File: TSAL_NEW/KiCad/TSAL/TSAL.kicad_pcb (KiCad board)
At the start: 2 copper layers, 101.6 x 25.4 mm, 0 parts

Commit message: Ready for Review
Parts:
- added C1: 1u, Capacitor_SMD:C_0603_1608Metric_Pad1.05x0.95mm_HandSolder, F.Cu at (174.5, 113.7)
- added C2: 1u, Capacitor_SMD:C_0603_1608Metric_Pad1.05x0.95mm_HandSolder, F.Cu at (174.6, 115.4)
- added J1: HV INPUT, Connector_TE-Connectivity:TE_MATE-N-LOK_1-770866-x_1x02_P4.14mm_Vertical, F.Cu at (120.3, 94.0)
- added J2: HV GND, Connector_TE-Connectivity:TE_MATE-N-LOK_1-770866-x_1x02_P4.14mm_Vertical, F.Cu at (119.8, 120.9)
- added J3: Green_LED_Jp, Connector_TE-Connectivity:TE_MATE-N-LOK_1-770866-x_1x02_P4.14mm_Vertical, F.Cu at (178.4, 94.0)
- added J4: Conn_02x03_Counter_Clockwise, Connector_TE-Connectivity:TE_MATE-N-LOK_1-770875-x_2x03_P4.14mm_Vertical, F.Cu at (194.6, 103.4)
- added Q1: BSS84, Package_TO_SOT_SMD:SOT-23, F.Cu at (180.8, 113.9)
- added Q2: FDD8447L, Package_TO_SOT_SMD:TO-252-2, F.Cu at (196.2, 117.8)
- added R1: 10k, Resistor_SMD:R_0603_1608Metric_Pad1.05x0.95mm_HandSolder, F.Cu at (144.4, 123.7)
- added R2: 180k, Resistor_SMD:R_0603_1608Metric_Pad1.05x0.95mm_HandSolder, F.Cu at (136.8, 103.9)
- added R3: 20k, Resistor_SMD:R_0603_1608Metric_Pad1.05x0.95mm_HandSolder, F.Cu at (131.9, 103.9)
- added R4: 100k, Resistor_SMD:R_0603_1608Metric_Pad1.05x0.95mm_HandSolder, F.Cu at (183.1, 118.4)
- added R5: 235k, Resistor_SMD:R_0603_1608Metric_Pad1.05x0.95mm_HandSolder, F.Cu at (183.1, 122.0)
- added R6: R, Resistor_SMD:R_0603_1608Metric_Pad1.05x0.95mm_HandSolder, F.Cu at (182.5, 110.7)
- added R7: 10k, Resistor_SMD:R_0603_1608Metric_Pad1.05x0.95mm_HandSolder, F.Cu at (191.0, 121.7)
- added R8: 1k, Resistor_SMD:R_0603_1608Metric_Pad1.05x0.95mm_HandSolder, F.Cu at (190.9, 114.0)
- added U1: LTV-817S, Package_DIP:SMDIP-4_W9.53mm, F.Cu at (136.0, 121.7)
- added U2: LR8K4-G, Package_TO_SOT_SMD:TO-252-2, F.Cu at (135.1, 96.0)
- added U3: LM555, Package_SO:SOIC-8_3.9x4.9mm_P1.27mm, F.Cu at (177.0, 119.6)
- added U4: LDB-350L, aero_footprint:LDB-_L, F.Cu at (167.0, 93.1)
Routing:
- net +12V: track 0.00 -> 81.8 mm
- net /GLV+: track 0.00 -> 79.7 mm
- net +24V: track 0.00 -> 64.5 mm
- net GNDA: track 0.00 -> 38.0 mm
- net +12VA: track 0.00 -> 27.4 mm
- net /555_OUTPUT: track 0.00 -> 20.5 mm
- net /THR: track 0.00 -> 19.4 mm
- net /HV+: track 0.00 -> 14.8 mm
- net /LED_GREEN+: track 0.00 -> 12.5 mm
- net /LED_RED+: track 0.00 -> 10.3 mm
- net Net-(R2-Pad2): track 0.00 -> 9.45 mm
- net /DIS: track 0.00 -> 5.65 mm
- net Net-(Q2-Pad3): track 0.00 -> 3.70 mm
- net Net-(Q1-Pad3): track 0.00 -> 2.53 mm
- added copper zone on F.Cu, net GND
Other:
- board size 101.6 x 25.4 mm -> 96.5 x 40.6 mm
- net class HV added: clearance 0.85, trace_width 1.2, via_dia 1, via_drill 0.6
- board text added: "GLV"
- board text added: "HV+"
- board text added: "HV-"
- board text added: "TSV"

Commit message: Ready for Review
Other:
- board text added: "TSAL G.Spearing 20.0131"
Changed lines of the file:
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@@
   (general
     (thickness 1.6)
-    (drawings 18)
+    (drawings 19)
     (tracks 93)
     (zones 0)
@@
   )
   (setup
-    (last_trace_width 0.65)
+    (last_trace_width 0.25)
     (user_trace_width 0.24)
     (user_trace_width 0.36)
@@
     (add_net +12V)
     (add_net +24V)
-    (add_net /12V)
     (add_net /555_OUTPUT)
     (add_net /DIS)
@@
     (add_net "Net-(Q2-Pad3)")
     (add_net "Net-(R2-Pad2)")
-    (add_net "Net-(U3-Pad5)")
-    (add_net "Net-(U4-Pad21)")
   )
   (net_class HV ""
@@
     )
   )
+  (gr_text "TSAL\nG.Spearing\n20.0131" (at 191.77 120.65) (layer B.SilkS)
+    (effects (font (size 1 1) (thickness 0.15)) (justify mirror))
+  )
   (gr_line (start 136.398 126.619) (end 136.398 118.364) (layer F.SilkS) (width 0.5))

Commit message: Ready for Reivew
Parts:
- added G***: LOGO, aero_footprint:AERO_Logo_25x10mm, B.Cu at (175.0, 110.7)
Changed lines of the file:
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@@
     (tracks 93)
     (zones 0)
-    (modules 20)
+    (modules 21)
     (nets 16)
   )
@@
     (add_net GNDA)
   )
+  (module aero_footprint:AERO_Logo_25x10mm (layer B.Cu)
+    (at 175.006 110.744 180)
+    (fp_text reference G*** (at 0 0) (layer B.SilkS) hide
+      (effects (font (size 1.524 1.524) (thickness 0.3)) (justify mirror))
+    )
+    (fp_text value LOGO (at 0.75 0) (layer B.SilkS) hide
+      (effects (font (size 1.524 1.524) (thickness 0.3)) (justify mirror))
+    )
+    (fp_poly (pts (xy 12.525229 2.710159) (xy 12.525229 -2.535324) (xy 10.339393 -4.71889) (xy 9.364192 -3.742421)
+      (xy 8.388991 -2.765953) (xy 8.388991 -2.2956) (xy 9.845413 -2.2956) (xy 10.032432 -2.488555)
+      (xy 10.219452 -2.68151) (xy 11.01055 -1.896474) (xy 11.01055 2.012048) (xy 10.427982 2.592431)
+      (xy 9.845413 3.172814) (xy 9.845413 -2.2956) (xy 8.388991 -2.2956) (xy 8.388991 2.76845)
+      (xy 9.408495 3.786706) (xy 10.427999 4.804961) (xy 12.525229 2.710159)) (layer B.SilkS) (width 0.01))
+    (fp_poly (pts (xy 6.802244 3.946175) (xy 7.631651 3.115285) (xy 7.631651 1.604369) (xy 7.123086 1.093437)
+      (xy 6.614521 0.582504) (xy 7.152215 0.042566) (xy 7.689908 -0.497373) (xy 7.689908 -2.763538)
+      (xy 7.994602 -3.072064) (xy 8.299295 -3.38059) (xy 6.960436 -4.719449) (xy 6.307049 -4.063738)
+      (xy 5.653662 -3.408028) (xy 6.228442 -2.767202) (xy 6.233486 -1.250536) (xy 5.592661 -0.611697)
+      (xy 4.951835 0.027141) (xy 4.951835 -2.829839) (xy 5.243762 -3.117377) (xy 5.53569 -3.404915)
+      (xy 4.880607 -4.061861) (xy 4.656022 -4.284832) (xy 4.45981 -4.475378) (xy 4.306705 -4.619528)
+      (xy 4.21144 -4.703309) (xy 4.187859 -4.718807) (xy 4.136831 -4.678799) (xy 4.020352 -4.568311)
+      (xy 3.852889 -4.401644) (xy 3.648913 -4.193102) (xy 3.512625 -4.05132) (xy 2.875057 -3.383832)
+      (xy 3.495413 -2.771182) (xy 3.495413 0.787039) (xy 4.835321 0.787039) (xy 6.3203 2.272018)
+      (xy 5.577811 3.014508) (xy 4.835321 3.756998) (xy 4.835321 0.787039) (xy 3.495413 0.787039)
+      (xy 3.495413 2.938594) (xy 3.161895 3.275628) (xy 2.828378 3.612662) (xy 3.98841 4.777064)
+      (xy 5.972837 4.777064) (xy 6.802244 3.946175)) (layer B.SilkS) (width 0.01))
+    (fp_poly (pts (xy -2.477659 2.622121) (xy -3.029276 2.068201) (xy -3.580892 1.514282) (xy -5.184862 3.115182)
+      (xy -5.184862 0.69421) (xy -4.078692 0.711211) (xy -2.972522 0.728211) (xy -4.396646 -0.699083)
+      (xy -5.184862 -0.699083) (xy -5.184862 -2.382603) (xy -4.977207 -2.540989) (xy -4.769551 -2.699376)
+      (xy -4.175481 -2.107328) (xy -3.581411 -1.515279) (xy -2.530301 -2.566389) (xy -3.611941 -3.642598)
+      (xy -3.902517 -3.930701) (xy -4.165689 -4.189694) (xy -4.390326 -4.40878) (xy -4.565301 -4.577165)
+      (xy -4.679482 -4.684053) (xy -4.72142 -4.718807) (xy -4.768729 -4.679379) (xy -4.886204 -4.568805)
+      (xy -5.061953 -4.398654) (xy -5.284083 -4.180497) (xy -5.540701 -3.925902) (xy -5.695272 -3.77149)
+      (xy -6.641284 -2.824173) (xy -6.641284 2.704844) (xy -5.623333 3.72851) (xy -4.605381 4.752177)
+      (xy -2.477659 2.622121)) (layer B.SilkS) (width 0.01))
+    (fp_poly (pts (xy -8.694247 3.771558) (xy -7.689908 2.765987) (xy -7.689908 -2.763538) (xy -7.385215 -3.072064)
+      (xy -7.080521 -3.38059) (xy -7.749951 -4.050019) (xy -8.41938 -4.719449) (xy -9.755082 -3.379947)
+      (xy -9.450706 -3.071743) (xy -9.14633 -2.763538) (xy -9.14633 -1.572936) (xy -10.427982 -1.572936)
+      (xy -10.427982 -2.763538) (xy -10.123288 -3.072064) (xy -9.818595 -3.38059) (xy -11.157454 -4.719449)
+      (xy -11.825305 -4.049698) (xy -12.493155 -3.379947) (xy -12.18878 -3.071743) (xy -11.884404 -2.763538)
+      (xy -11.884404 -0.058257) (xy -10.427982 -0.058257) (xy -9.14633 -0.058257) (xy -9.14633 1.838329)
+      (xy -9.784204 2.506665) (xy -10.422078 3.175) (xy -10.42503 1.558371) (xy -10.427982 -0.058257)
+      (xy -11.884404 -0.058257) (xy -11.884404 2.593581) (xy -10.791495 3.685355) (xy -9.698586 4.777128)
+      (xy -8.694247 3.771558)) (layer B.SilkS) (width 0.01))
+    (fp_poly (pts (xy 1.48555 3.437156) (xy 0.88742 1.805963) (xy 1.792647 1.805963) (xy 2.13411 1.805266)
+      (xy 2.374206 1.801911) (xy 2.528081 1.794001) (xy 2.610878 1.779642) (xy 2.637744 1.756938)
+      (xy 2.623822 1.723993) (xy 2.607124 1.704014) (xy 2.560496 1.642703) (xy 2.452739 1.496064)
+      (xy 2.2906 1.273472) (xy 2.080823 0.984301) (xy 1.830152 0.637926) (xy 1.545334 0.243722)
+      (xy 1.233113 -0.188937) (xy 0.900234 -0.650674) (xy 0.553443 -1.132116) (xy 0.199483 -1.623887)
+      (xy -0.154899 -2.116613) (xy -0.502959 -2.600919) (xy -0.837952 -3.06743) (xy -1.153132 -3.506771)
+      (xy -1.441755 -3.909568) (xy -1.697076 -4.266444) (xy -1.912349 -4.568027) (xy -2.08083 -4.80494)
+      (xy -2.195773 -4.967808) (xy -2.250434 -5.047258) (xy -2.251631 -5.049138) (xy -2.247031 -5.018182)
+      (xy -2.207458 -4.887527) (xy -2.136353 -4.667475) (xy -2.037157 -4.368325) (xy -1.913312 -4.000379)
+      (xy -1.768257 -3.573937) (xy -1.605433 -3.099301) (xy -1.450599 -2.651135) (xy -1.272624 -2.137289)
+      (xy -1.106931 -1.658286) (xy -0.957313 -1.225136) (xy -0.827562 -0.84885) (xy -0.721473 -0.540437)
+      (xy -0.642839 -0.310908) (xy -0.595452 -0.171273) (xy -0.582569 -0.131524) (xy -0.637453 -0.126278)
+      (xy -0.788619 -0.121831) (xy -1.015833 -0.118534) (xy -1.298863 -0.116739) (xy -1.448313 -0.116514)
+      (xy -2.314057 -0.116514) (xy -1.663387 1.354472) (xy -1.457671 1.81999) (xy -1.235644 2.323191)
+      (xy -1.011221 2.832488) (xy -0.798318 3.316289) (xy -0.610849 3.743005) (xy -0.521442 3.946904)
+      (xy -0.030166 5.068348) (xy 2.083681 5.068348) (xy 1.48555 3.437156)) (layer B.SilkS) (width 0.01))
+  )
   (module Connector_TE-Connectivity:TE_MATE-N-LOK_1-770866-x_1x02_P4.14mm_Vertical (layer F.Cu)

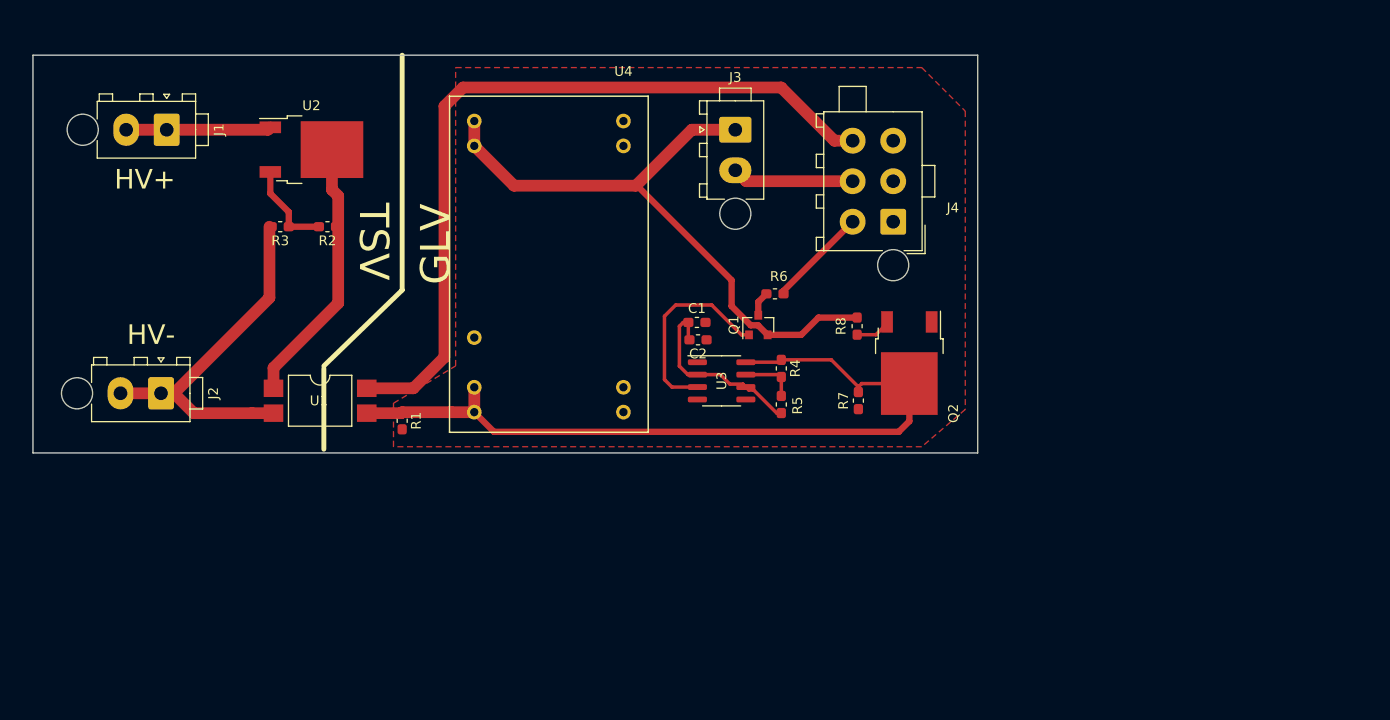
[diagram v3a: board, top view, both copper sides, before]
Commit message: Final Schem - No Boost
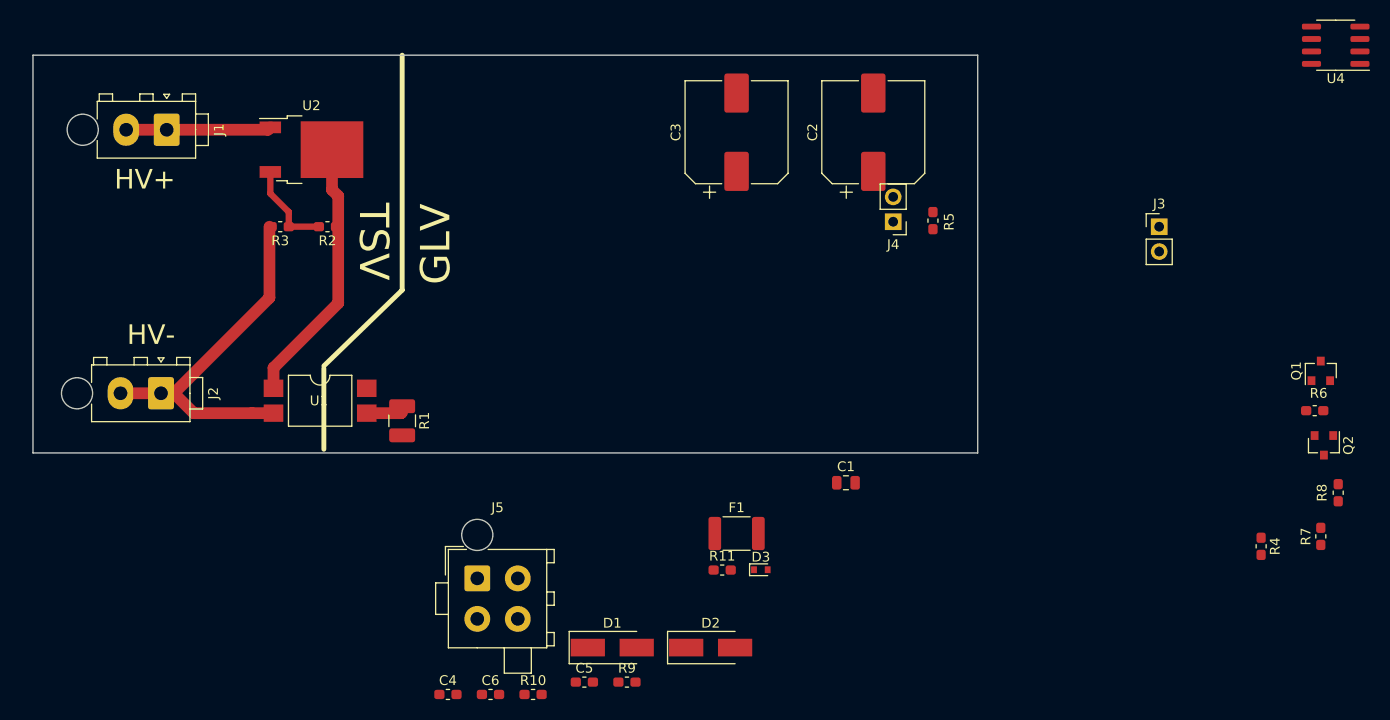
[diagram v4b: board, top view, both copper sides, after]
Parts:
- removed G***: LOGO, aero_footprint:AERO_Logo_25x10mm
- removed U3: LM555, Package_SO:SOIC-8_3.9x4.9mm_P1.27mm
- added C3: 330uF, Capacitor_SMD:CP_Elec_10x10, F.Cu at (178.6, 94.2)
- added C4: 1u, Capacitor_SMD:C_0603_1608Metric_Pad1.05x0.95mm_HandSolder, F.Cu at (149.1, 151.7)
- added C5: 1u, Capacitor_SMD:C_0603_1608Metric_Pad1.05x0.95mm_HandSolder, F.Cu at (163.0, 150.4)
- added C6: 0.1uF, Capacitor_SMD:C_0603_1608Metric_Pad1.05x0.95mm_HandSolder, F.Cu at (153.4, 151.7)
- added D1: B340A-13-F1, Diode_SMD:D_SMA_Handsoldering, F.Cu at (165.9, 146.9)
- added D2: ESD5Z12T1G, Diode_SMD:D_SMA_Handsoldering, F.Cu at (175.9, 146.9)
- added D3: 1N4148WT, Diode_SMD:D_SOD-523, F.Cu at (181.0, 138.9)
- added F1: 1812L075/24, Fuse:Fuse_1812_4532Metric_Pad1.30x3.40mm_HandSolder, F.Cu at (178.6, 135.2)
- added J5: Conn_02x02_Counter_Clockwise, Connector_TE-Connectivity:TE_MATE-N-LOK_1-770874-x_2x02_P4.14mm_Vertical, F.Cu at (152.1, 139.8)
- added R10: 100, Resistor_SMD:R_0603_1608Metric_Pad1.05x0.95mm_HandSolder, F.Cu at (157.8, 151.7)
- added R11: 10k, Resistor_SMD:R_0603_1608Metric_Pad1.05x0.95mm_HandSolder, F.Cu at (177.1, 139.0)
- added R9: 10k, Resistor_SMD:R_0603_1608Metric_Pad1.05x0.95mm_HandSolder, F.Cu at (167.4, 150.4)
- C1: value 1u -> C2012X7S2A105K125AB; footprint Capacitor_SMD:C_0603_1608Metric_Pad1.05x0.95mm_HandSolder -> Capacitor_SMD:C_0805_2012Metric
- C2: value 1u -> 330uF; footprint Capacitor_SMD:C_0603_1608Metric_Pad1.05x0.95mm_HandSolder -> Capacitor_SMD:CP_Elec_10x10
- J3: value Green_LED_Jp -> Pin Storage; footprint Connector_TE-Connectivity:TE_MATE-N-LOK_1-770866-x_1x02_P4.14mm_Vertical -> Connector_PinHeader_2.54mm:PinHeader_1x02_P2.54mm_Vertical
- J4: value Conn_02x03_Counter_Clockwise -> Green_LED_Jp; footprint Connector_TE-Connectivity:TE_MATE-N-LOK_1-770875-x_2x03_P4.14mm_Vertical -> Connector_PinHeader_2.54mm:PinHeader_1x02_P2.54mm_Vertical
- Q2: value FDD8447L -> BSS84; footprint Package_TO_SOT_SMD:TO-252-2 -> Package_TO_SOT_SMD:SOT-23
- R1: value 10k -> 549; footprint Resistor_SMD:R_0603_1608Metric_Pad1.05x0.95mm_HandSolder -> Resistor_SMD:R_1210_3225Metric_Pad1.42x2.65mm_HandSolder
- R2: value 180k -> 10k
- R3: value 20k -> 180k
- R4: value 100k -> 20k
- R5: value 235k -> 2
- R6: value R -> 100k
- R7: value 10k -> 235k
- R8: value 1k -> 100
- U4: value LDB-350L -> LM555; footprint aero_footprint:LDB-_L -> Package_SO:SOIC-8_3.9x4.9mm_P1.27mm
- moved U4 73.2 mm to (239.8, 85.3)
- moved Q1 57.7 mm to (238.3, 118.6)
- moved R6 56.4 mm to (237.6, 122.7)
- moved R4 52.3 mm to (232.2, 136.5)
- moved R8 52.0 mm to (240.0, 131.1)
- moved R7 49.2 mm to (238.3, 135.5)
- moved J3 44.4 mm to (221.7, 103.9)
- moved Q2 43.2 mm to (238.6, 126.2)
- moved C2 27.8 mm to (192.5, 94.2), turned to 90 degrees
- moved R5 24.3 mm to (198.6, 103.3)
- moved C1 22.4 mm to (189.7, 130.0)
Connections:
- C1 pad 1: /THR -> +12VA
- C1 pad 2: GND -> GNDA
- C2 pad 1: GND -> /12V_CAP
- C2 pad 2: /THR -> GND
- J3 pad 1: +24V -> (no net)
- J3 pad 2: /LED_GREEN+ -> (no net)
- J4 pad 1: GND -> (no net)
- J4 pad 2: GND -> /LED_GREEN+
- Q1 pad 1: /555_OUTPUT -> Net-(Q1-Pad1)
- Q1 pad 3: Net-(Q1-Pad3) -> /LED_GREEN+
- Q2 pad 1: GND -> /RED_FET
- Q2 pad 2: +12V -> +24V
- Q2 pad 3: Net-(Q2-Pad3) -> /LED_RED+
- R1 pad 1: +12V -> +12VA
- R1 pad 2: GND -> Net-(R1-Pad2)
- R2 pad 1: +12VA -> /HV_PRES
- R2 pad 2: Net-(R2-Pad2) -> GND
- R3 pad 1: Net-(R2-Pad2) -> +12VA
- R3 pad 2: GNDA -> Net-(R3-Pad2)
- R4 pad 1: +12V -> Net-(R3-Pad2)
- R4 pad 2: /DIS -> GNDA
- R5 pad 1: /DIS -> /12V_CAP
- R5 pad 2: /THR -> +12V
- R6 pad 1: /LED_RED+ -> +12V
- R6 pad 2: Net-(Q1-Pad3) -> /DIS
- R7 pad 1: +12V -> /DIS
- R7 pad 2: GND -> /THR
- R8 pad 1: +24V -> Net-(Q1-Pad1)
- R8 pad 2: Net-(Q2-Pad3) -> Net-(D3-Pad1)
- U1 pad 1: +12VA -> Net-(R1-Pad2)
- U1 pad 3: +12V -> /HV_PRES
- U1 pad 4: /GLV+ -> +12V
- U2 pad 3: Net-(R2-Pad2) -> Net-(R3-Pad2)
- U4 pad 2: GND -> /THR
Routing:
- net /GLV+: track 79.7 -> 0.00 mm
- net +12V: track 81.8 -> 3.66 mm
- net +24V: track 64.5 -> 0.00 mm
- net /555_OUTPUT: track 20.5 -> 0.00 mm
- net /THR: track 19.4 -> 0.00 mm
- net /LED_GREEN+: track 12.5 -> 0.00 mm
- net /LED_RED+: track 10.3 -> 0.00 mm
- net /DIS: track 5.65 -> 0.00 mm
- net Net-(Q2-Pad3): track 3.70 -> 0.00 mm
- net Net-(Q1-Pad3): track 2.53 -> 0.00 mm
- removed copper zone on F.Cu, net GND

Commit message: Final PCB
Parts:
- added H1: MountingHole, MountingHole:MountingHole_3mm, F.Cu at (144.8, 106.7)
- added H2: MountingHole, MountingHole:MountingHole_3mm, F.Cu at (113.8, 106.7)
- moved R4 106.6 mm to (131.0, 103.0), turned to 180 degrees
- moved U4 92.7 mm to (154.5, 121.6), turned to 0 degrees
- moved R8 92.6 mm to (149.0, 114.0)
- moved Q1 84.7 mm to (154.0, 110.0)
- moved Q2 83.3 mm to (156.0, 115.0), turned to 90 degrees
- moved R7 78.3 mm to (161.0, 122.9)
- moved R6 75.6 mm to (162.1, 119.0), turned to 0 degrees
- moved C1 65.7 mm to (126.0, 113.9), turned to 270 degrees
- moved J3 56.8 mm to (165.0, 105.0)
- moved D1 49.6 mm to (170.0, 97.5), turned to 90 degrees
- moved D2 49.4 mm to (175.0, 97.5), turned to 270 degrees
- moved J5 47.3 mm to (159.0, 93.0), turned to 270 degrees
- moved F1 45.9 mm to (171.0, 90.0), turned to 180 degrees
- moved R9 41.5 mm to (158.0, 110.0), turned to 270 degrees
- moved J4 38.6 mm to (156.0, 105.0), turned to 270 degrees
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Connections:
- J3 pad 1: (no net) -> Net-(J3-Pad1)
- J3 pad 2: (no net) -> Net-(J3-Pad2)
- J4 pad 1: (no net) -> /LED_GREEN_OUT
- Q1 pad 2: +24V -> +12V
- Q1 pad 3: /LED_GREEN+ -> /LED_GREEN_OUT
- Q2 pad 2: +24V -> +12V
- R9 pad 1: /LED_GREEN+ -> /LED_GREEN_OUT
- U4 pad 5: (no net) -> Net-(U4-Pad5)
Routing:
- net +12V: track 3.66 -> 76.3 mm, vias 0 -> 4
- net /12V_CAP: track 0.00 -> 32.0 mm
- net /LED_RED+: track 0.00 -> 28.0 mm
- net /THR: track 0.00 -> 14.1 mm
- net /HV_PRES: track 0.00 -> 12.3 mm
- net /GLV+: track 0.00 -> 11.8 mm
- net Net-(R3-Pad2): track 0.00 -> 10.8 mm
- net Net-(R2-Pad2): track 9.45 -> 0.00 mm
- net GNDA: track 38.0 -> 47.4 mm
- net /LED_GREEN_OUT: track 0.00 -> 9.04 mm
- net /RED_FET: track 0.00 -> 9.00 mm
- net Net-(D3-Pad1): track 0.00 -> 8.53 mm
- net /LED_GREEN+: track 0.00 -> 8.44 mm
- net /DIS: track 0.00 -> 8.24 mm
- net Net-(D1-Pad2): track 0.00 -> 6.34 mm
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- added copper zone on B.Cu, net GND
- added copper zone on F.Cu, net GND
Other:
- board size 96.5 x 40.6 mm -> 74.8 x 41.9 mm
